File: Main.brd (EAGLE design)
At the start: 100 x 80 mm, 24 parts, among them IC1 PIC16F1939P, J1 EM-506-VERTICAL, Q6 IRFD9210

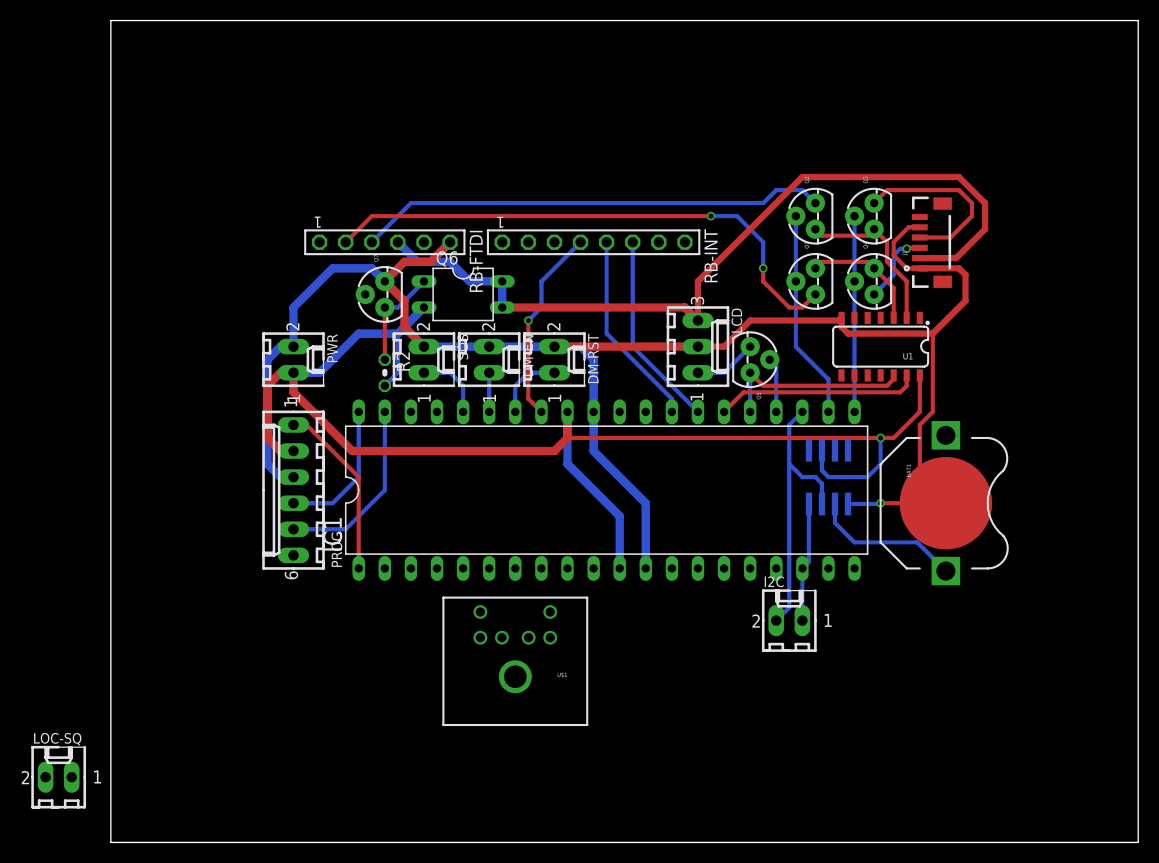
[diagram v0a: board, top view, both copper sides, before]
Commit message: Encrypter work
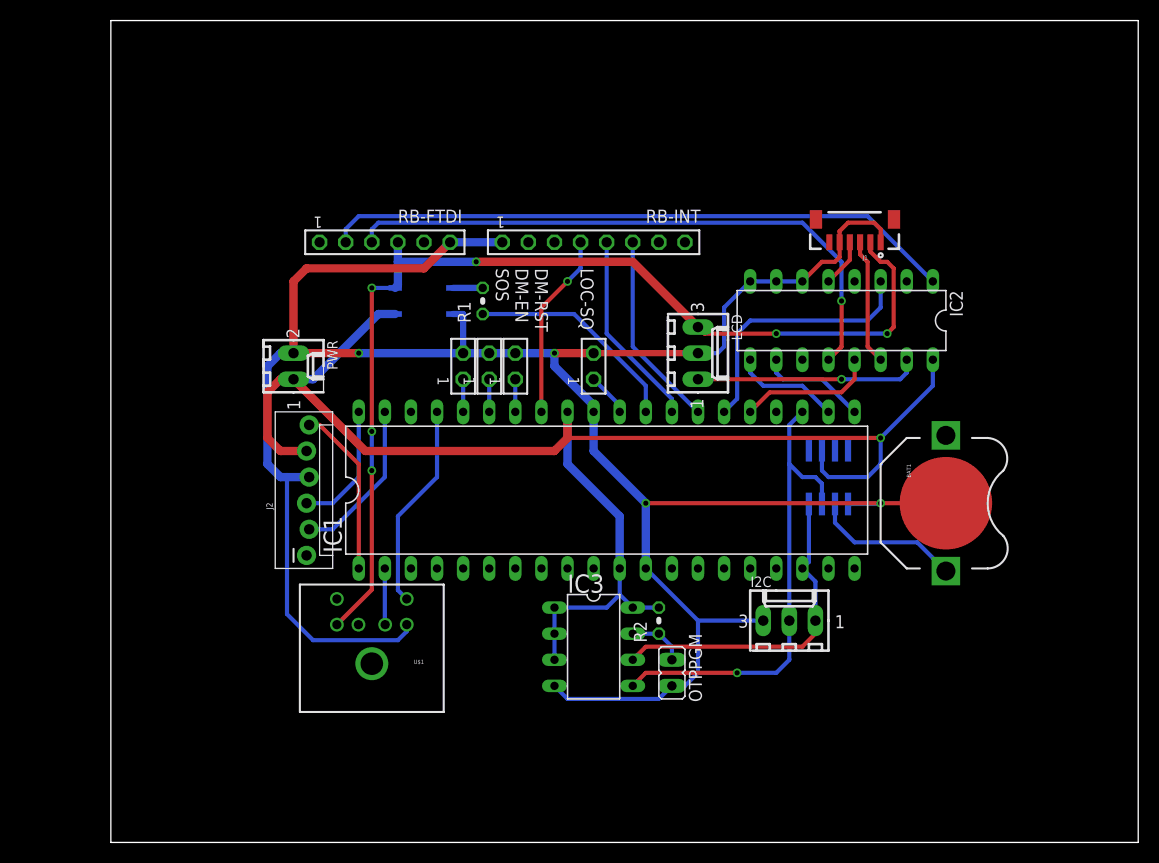
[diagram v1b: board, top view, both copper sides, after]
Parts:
- removed PROG: 22-27-2061-06, con-molex:6410-06
- removed Q1, Q2, Q3, Q4, Q5, Q7: (no value), SparkFun-DiscreteSemi:TO-92
- removed Q6: IRFD9210, transistor-fet:DIL04
- removed U1: (no value), SparkFun-DigitalIC:SO14
- added IC2: 4052N, 40xx:DIL16
- added IC3: 24AA01P, microchip:DIL8
- added J2: PIC_ICSP_6_PINPOLAR_LOCK, SparkFun-Connectors:MOLEX-1X6_LOCK
- added OTPPGM: (no value), jumper:JP1
- added R1: (no value), resistor:0204V
- added U$2: CPC1008N, JSB2:SOP04
- DM-EN, DM-RST, LOC-SQ, SOS: value 22-27-2021-02 -> TSW-102-02-S-S; device con-molex:6410-02 -> con-samtec:TSW-102-02-S-S
- I2C: value 22-27-2021-02 -> 22-27-2031-03; device con-molex:6410-02 -> con-molex:6410-03
- moved LOC-SQ 65.7 mm to (47.0, 46.4), turned to 270 degrees
- moved R2 36.0 mm to (53.3, 21.6), turned to 90 degrees
- moved U$1 14.0 mm to (25.4, 12.7)
- moved J1 4.58 mm to (74.9, 58.4), turned to 180 degrees
- moved DM-RST 3.86 mm to (39.4, 46.4)
- moved SOS 3.86 mm to (34.3, 46.4)
- moved DM-EN 0.64 mm to (36.8, 46.4)
- moved PWR 0.64 mm to (17.8, 46.4)
- moved LCD 0.63 mm to (57.1, 47.6)
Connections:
- removed net N$25: IC1.24, Q5.2
- new net N$27: IC3.7, OTPPGM.2, R2.1
- new net N$28: IC1.1, J2.6
- net +5V: now also IC2.16, IC3.1, IC3.2, IC3.3, IC3.8, J2.5, U$2.4; no longer PROG.2, Q6.2, U1.14
- net GND: now also I2C.3, IC2.6, IC2.7, IC2.8, IC3.4, J2.4, OTPPGM.1, RB-INT.1, U$1.3, U$2.3; no longer PROG.3, Q7.3, U1.7
- net N$1: now also IC2.3; no longer U1.13
- net N$10: now also IC2.5, J1.4; no longer Q1.1, RB-FTDI.2
- net N$11: now also IC2.9; no longer Q1.2, Q2.2
- net N$12: now also IC2.15, LCD.1; no longer J1.4, Q3.3
- net N$13: now also IC2.10; no longer Q3.2, Q4.2
- net N$14: now also IC1.37, U$1.5; no longer J1.3, Q4.1
- net N$15: now also IC1.39, J2.2; no longer IC1.1, PROG.1
- net N$16: now also J2.3; no longer PROG.4
- net N$17: now also R1.2, U$2.1; no longer IC1.39, PROG.5
- net N$2: now also IC2.13; no longer Q5.3, U1.12
- net N$24: now also IC1.2, U$1.1; no longer LCD.1, Q5.1
- net N$26: now also IC1.29, R1.1; no longer Q6.1, Q7.1, R2.1
- net N$3: now also IC3.6
- net N$4: now also IC3.5
- net N$5: now also IC1.30; no longer IC1.37
- net N$7: now also IC2.12, RB-FTDI.3; no longer Q2.1, Q3.1, U1.2
- net N$8: now also IC2.1, RB-FTDI.2; no longer Q1.3, Q4.3, U1.3
- net N$9: now also IC2.14, J1.3; no longer Q2.3, RB-FTDI.3
- net VPP: now also U$1.4, U$2.6; no longer Q6.3, Q6.4
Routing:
- net GND: track 171.4 -> 236.8 mm, vias 1 -> 4
- net N$8: track 11.9 -> 61.6 mm
- net N$10: track 53.2 -> 4.67 mm, vias 2 -> 0
- net N$7: track 16.2 -> 58.9 mm, vias 0 -> 1
- net N$9: track 45.8 -> 12.3 mm
- net VPP: track 80.9 -> 102.0 mm, vias 0 -> 6
- net N$3: track 11.6 -> 32.2 mm
- net N$4: track 27.3 -> 46.9 mm, vias 0 -> 1
- net N$28: track 0.00 -> 16.6 mm
- net N$17: track 18.1 -> 2.91 mm
- net N$14: track 7.44 -> 20.1 mm, vias 1 -> 0
- net N$26: track 9.94 -> 21.3 mm
- net +5V: track 133.4 -> 144.4 mm
- net N$11: track 20.4 -> 10.5 mm
- net N$13: track 19.1 -> 10.5 mm
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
